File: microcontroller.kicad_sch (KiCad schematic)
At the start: 52 parts, among them J1 Conn_01x06, J2 Conn_01x06, J3 47219-2001, SW1 SW_Push, U1 TPS7B88, U2 MCP1700x-330xxMB, U3 STM32F103C8Tx, U4 SN65HVD1050D, U5 TCA9535PWR, Y1 8M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

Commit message: schematic: Cleanup BOM
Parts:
- C19: DigiKey # 490-GQM1875C2E300GB12DCT-ND -> (none)
- J1: DigiKey # (none) -> 900-2125280600-ND; Mouser # (none) -> 538-212528-0600
- J3: DigiKey # (none) -> WM6698CT-ND; LCSC # (none) -> C164170; Mouser # (none) -> 538-47219-2001
- U5: DigiKey # (none) -> 296-25129-1-ND; LCSC # (none) -> C130204; Mfr (none) -> Texas Instruments; Mfr # (none) -> TCA9535PWR; Mouser # (none) -> 595-TCA9535PWR
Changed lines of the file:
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@@
 			)
 		)
-		(property "DigiKey #" "490-GQM1875C2E300GB12DCT-ND"
+		(property "DigiKey #" ""
 			(at 254 34.29 90)
 			(effects
@@
 			)
 		)
+		(property "DigiKey #" "296-25129-1-ND"
+			(at 161.29 58.42 0)
+			(effects
+				(font
+					(size 1.27 1.27)
+				)
+				(hide yes)
+			)
+		)
+		(property "LCSC #" "C130204"
+			(at 161.29 58.42 0)
+			(effects
+				(font
+					(size 1.27 1.27)
+				)
+				(hide yes)
+			)
+		)
+		(property "Mfr" "Texas Instruments"
+			(at 161.29 58.42 0)
+			(effects
+				(font
+					(size 1.27 1.27)
+				)
+				(hide yes)
+			)
+		)
+		(property "Mfr #" "TCA9535PWR"
+			(at 161.29 58.42 0)
+			(effects
+				(font
+					(size 1.27 1.27)
+				)
+				(hide yes)
+			)
+		)
+		(property "Mouser #" "595-TCA9535PWR"
+			(at 161.29 58.42 0)
+			(effects
+				(font
+					(size 1.27 1.27)
+				)
+				(hide yes)
+			)
+		)
 		(pin "18"
 		)
@@
 			)
 		)
+		(property "DigiKey #" "900-2125280600-ND"
+			(at 54.61 173.99 0)
+			(effects
+				(font
+					(size 1.27 1.27)
+				)
+				(hide yes)
+			)
+		)
+		(property "Mouser #" "538-212528-0600"
+			(at 54.61 173.99 0)
+			(effects
+				(font
+					(size 1.27 1.27)
+				)
+				(hide yes)
+			)
+		)
 		(pin "3"
 		)
@@
 			(at 236.22 39.37 0)
 			(effects
+				(font
+					(size 1.27 1.27)
+				)
+				(hide yes)
+			)
+		)
+		(property "DigiKey #" "WM6698CT-ND"
+			(at 236.22 39.37 0)
+			(effects
+				(font
+					(size 1.27 1.27)
+				)
+				(hide yes)
+			)
+		)
+		(property "LCSC #" "C164170"
+			(at 236.22 39.37 0)
+			(effects
+				(font
+					(size 1.27 1.27)
+				)
+				(hide yes)
+			)
+		)
+		(property "Mouser #" "538-47219-2001"
+			(at 236.22 39.37 0)
+			(effects

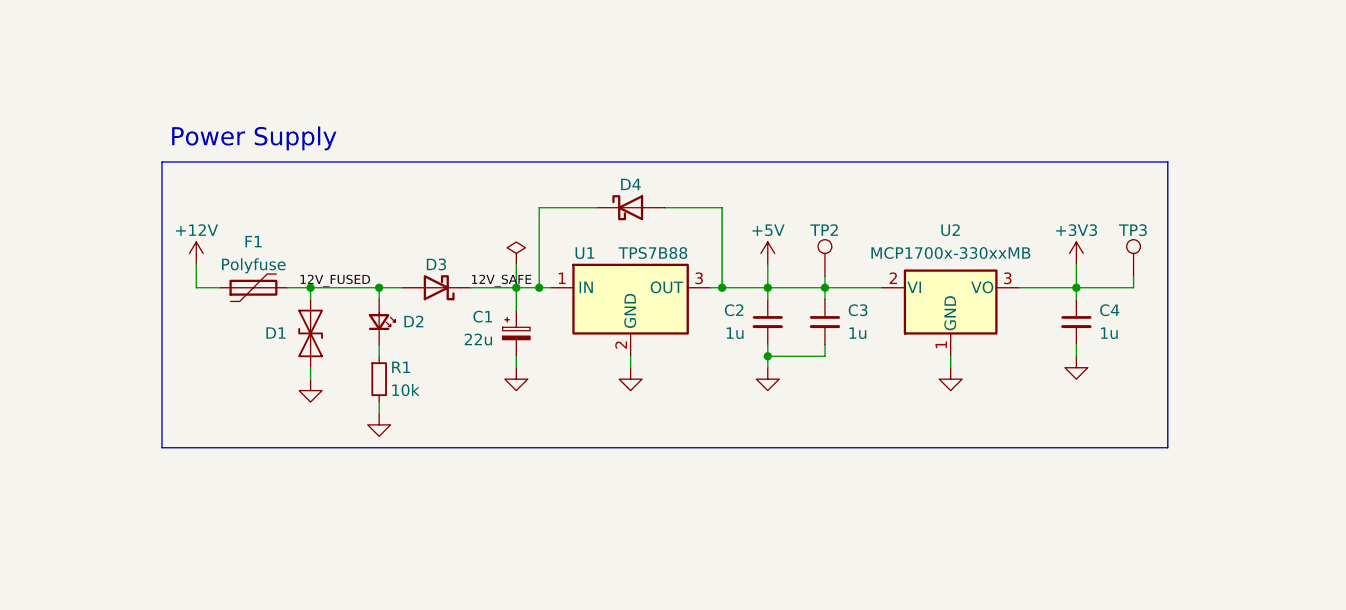
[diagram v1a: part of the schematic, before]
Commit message: schematic: Cleanup root schematic page
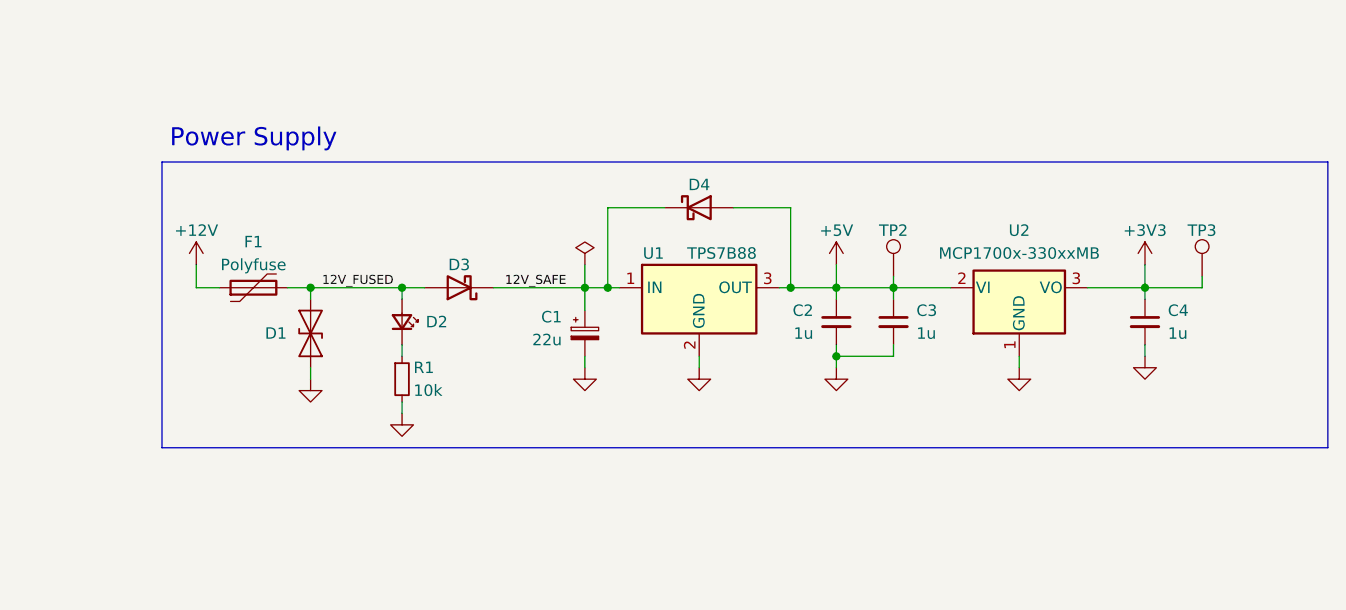
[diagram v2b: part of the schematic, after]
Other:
- moved on the sheet: C1, C2, C3, C4, D2, D3, D4, R1, TP2, TP3, U1, U2
